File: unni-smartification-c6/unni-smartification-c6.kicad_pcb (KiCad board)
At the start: 4 copper layers, 83.3 x 65 mm, 74 parts, among them J1 USB-C (replacement daughterbo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, J10 Conn_01x06, J2 Li-Ion 1S JST-PH, J3 Conn_01x06, J4 UNNI DC / battery input - AC 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, J5 Conn_01x02, J6 Conn_01x05, Q1 AO3401A, Q10 AO3400A touch emulator, Q2 AO3401A, Q3 AO3400A, Q4 AO3400A, SW1 RESET, SW2 BOOT, U1 MCP73831T-2ACI/OT, U10 ESP32-C6-MINI-1, U2 TPS63031DSK, U3 TPS613222ADBZ (5V), U4 TPD2E009DBZR

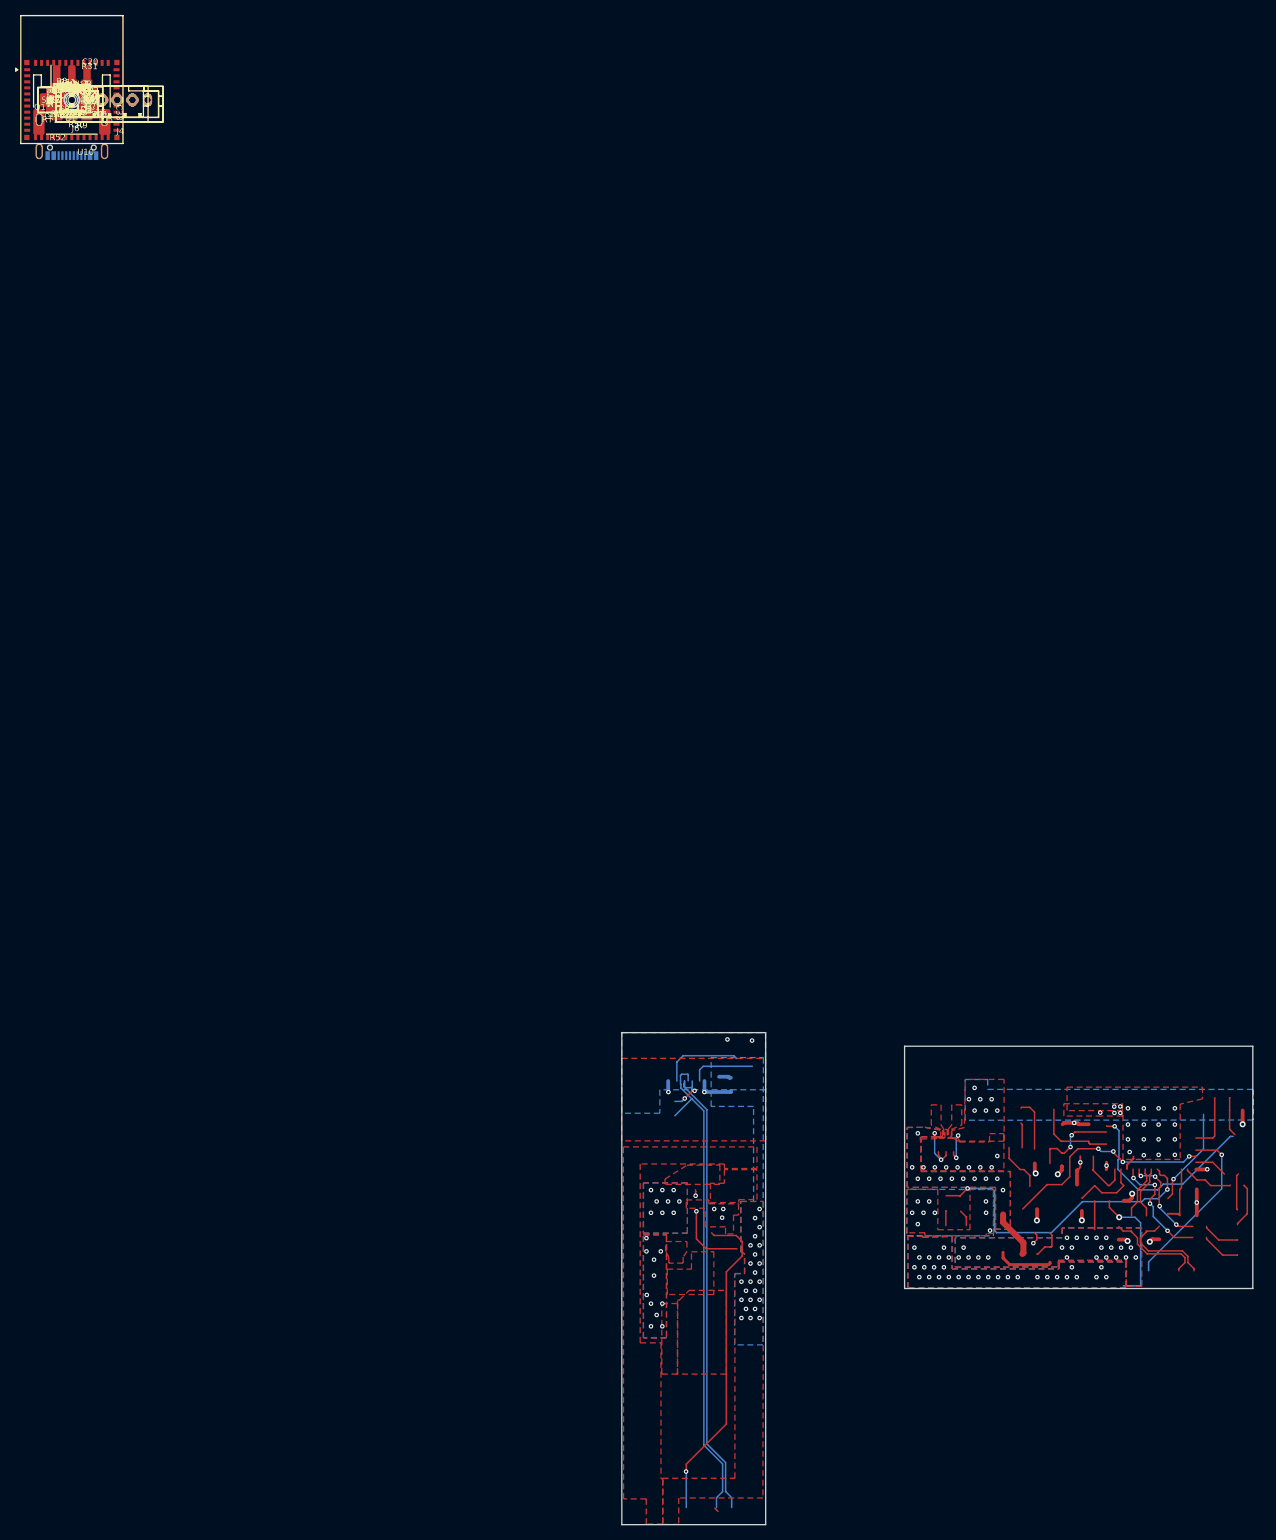
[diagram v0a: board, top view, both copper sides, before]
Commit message: beautify silkscreen on pcbs
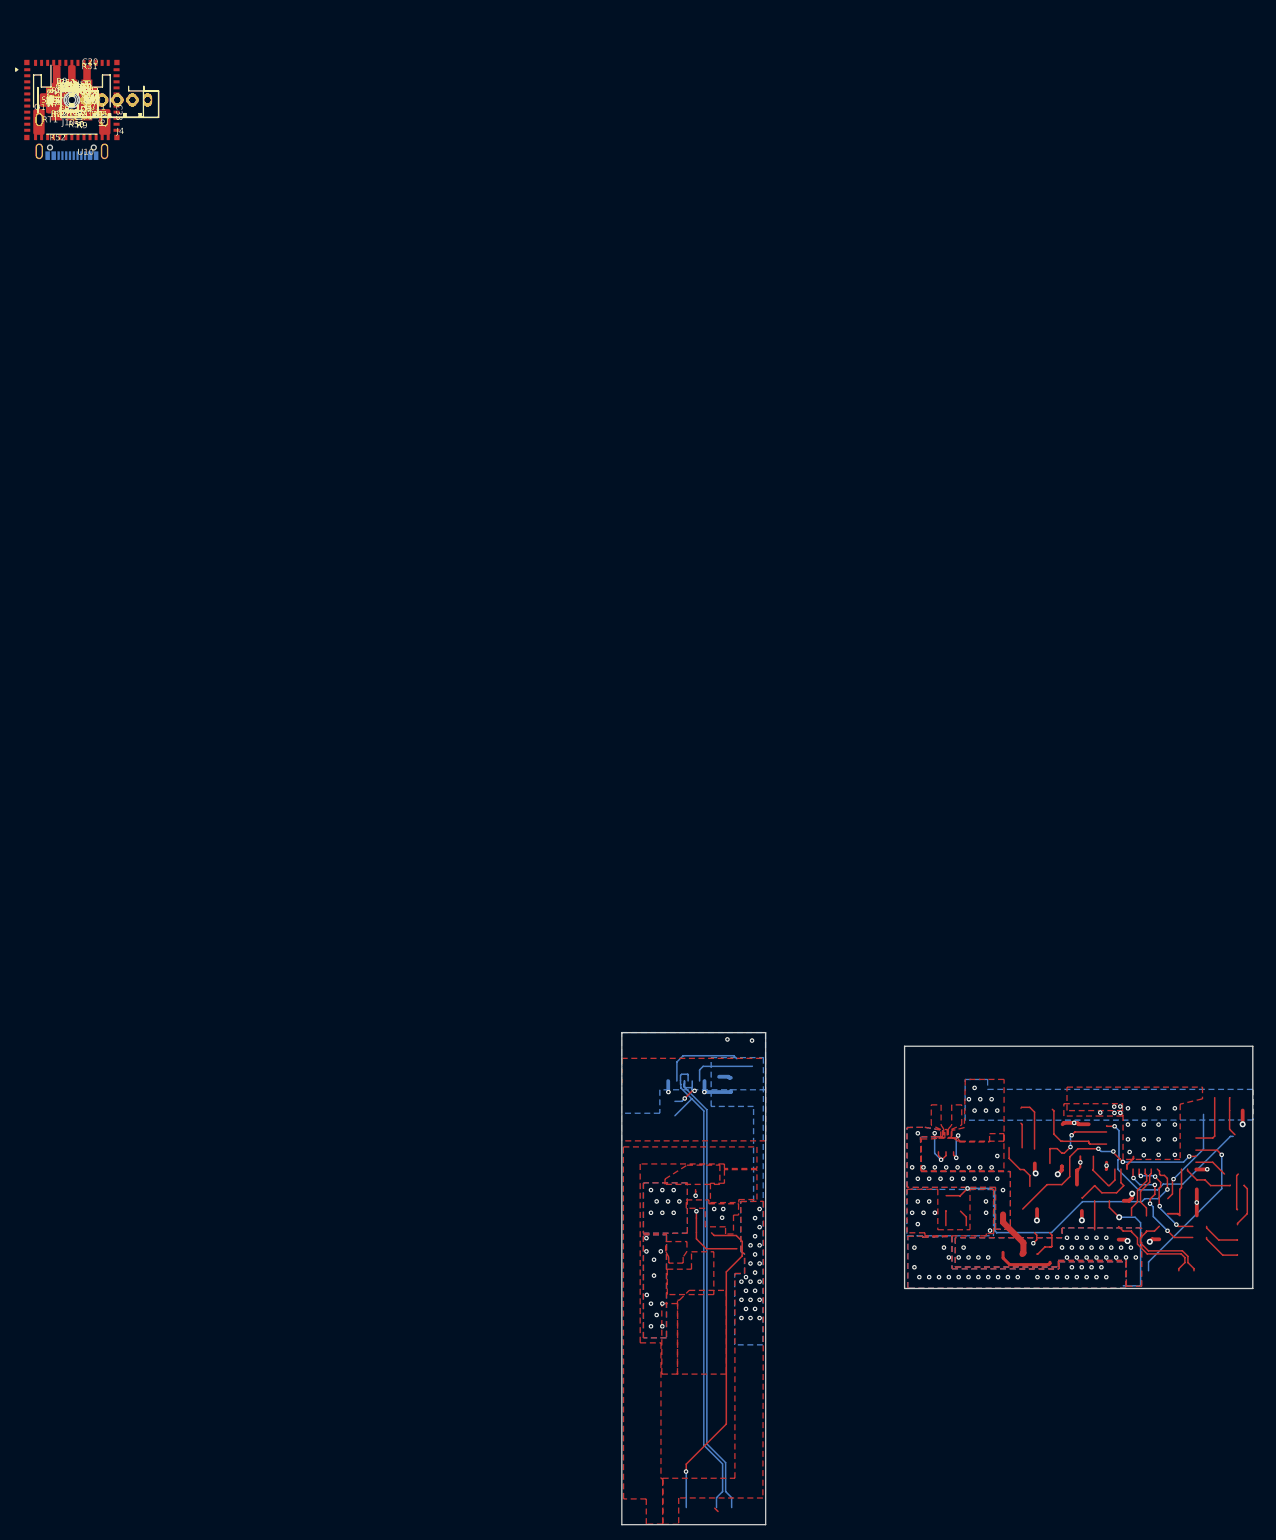
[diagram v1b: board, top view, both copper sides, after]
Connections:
- C13 pad 1: USB_RAW_P -> GND
- J1 pad A6: USB_RAW_P -> GND
- J1 pad B6: USB_RAW_P -> GND
- J10 pad 1: USB_RAW_P -> GND
- J3 pad 1: USB_RAW_P -> GND
- Q1 pad 1: Net-(Q1-G) -> SYS
- R23 pad 2: USB_RAW_P -> GND
- R5 pad 2: Net-(Q1-G) -> SYS
- R6 pad 2: Net-(Q1-G) -> SYS
- U4 pad 1: USB_RAW_P -> GND
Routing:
- net USB_RAW_P: track 78.7 -> 0.00 mm, vias 2 -> 0
- net GND: track 30.4 -> 109.1 mm, vias 63 -> 65
- net Net-(Q1-G): track 4.37 -> 0.00 mm
- net SYS: track 12.4 -> 16.8 mm
- net VBUS: vias 47 -> 52
- net +BATT: vias 31 -> 28

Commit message: silkscreen beautification
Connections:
- C13 pad 1: GND -> USB_RAW_P
- J1 pad A6: GND -> USB_RAW_P
- J1 pad B6: GND -> USB_RAW_P
- J10 pad 1: GND -> USB_RAW_P
- J3 pad 1: GND -> USB_RAW_P
- Q1 pad 1: SYS -> Net-(Q1-G)
- R23 pad 2: GND -> USB_RAW_P
- R5 pad 2: SYS -> Net-(Q1-G)
- R6 pad 2: SYS -> Net-(Q1-G)
- U4 pad 1: GND -> USB_RAW_P
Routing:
- net USB_RAW_P: track 0.00 -> 78.7 mm, vias 0 -> 2
- net GND: track 109.1 -> 30.4 mm, vias 65 -> 63
- net Net-(Q1-G): track 0.00 -> 4.37 mm
- net SYS: track 16.8 -> 12.4 mm
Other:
- board text added: "B-B+"
- board text added: "GND RT RH SDA SCL"
- board text added: "LED TOUCH"

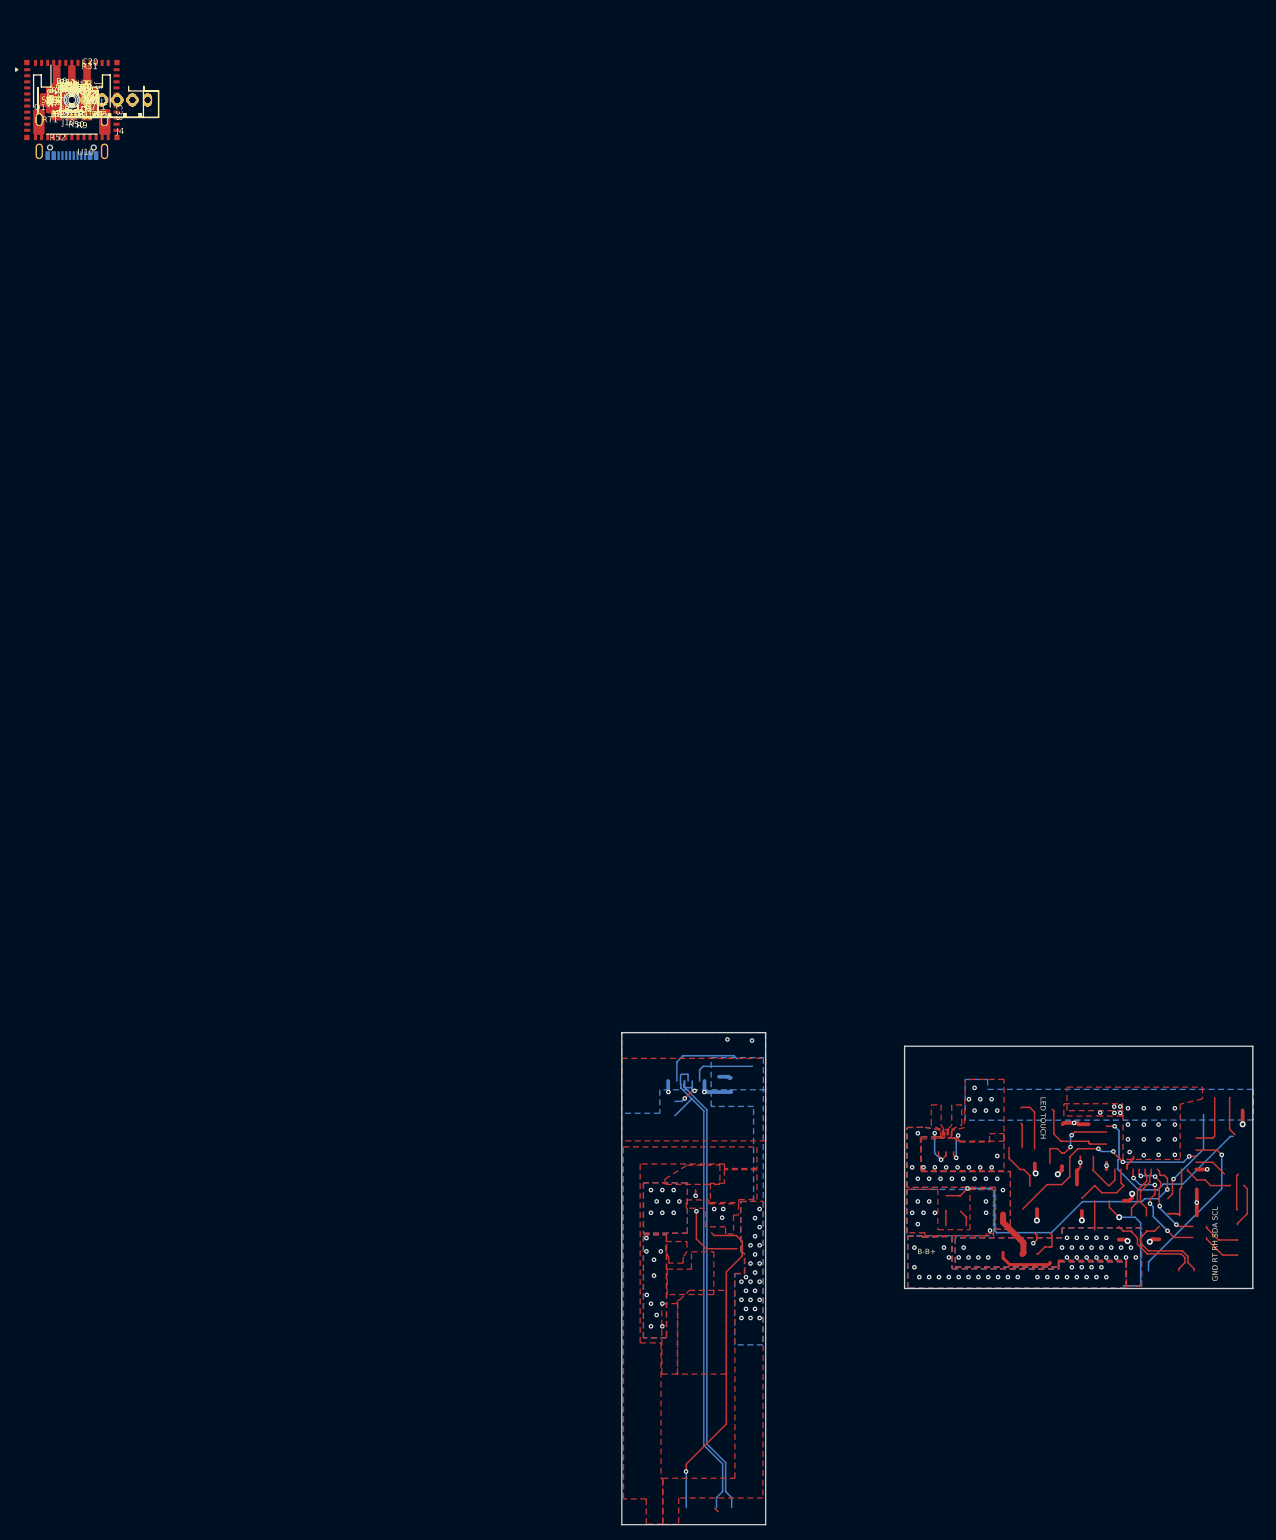
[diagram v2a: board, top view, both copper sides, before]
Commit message: redid some routing, add btn for manual measurements from unni
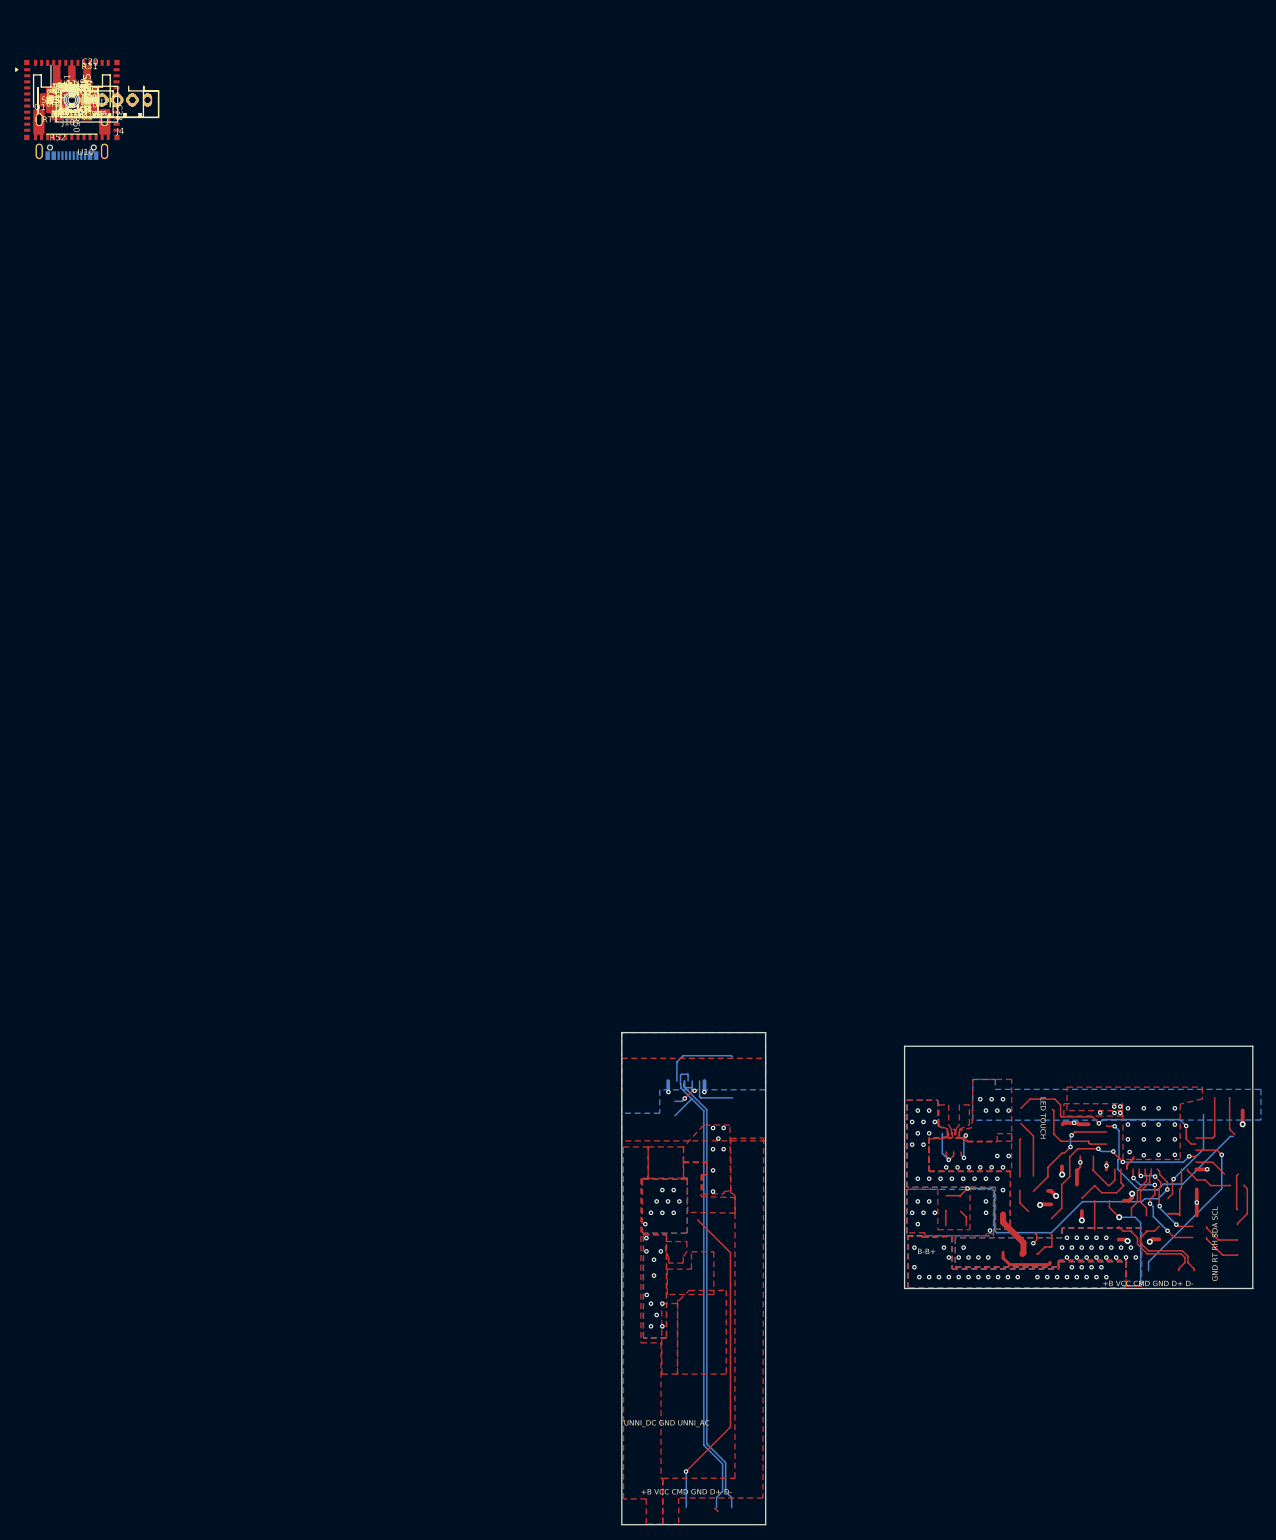
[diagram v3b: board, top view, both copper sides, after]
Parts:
- J5: footprint Connector_JST:JST_PH_B2B-PH-K_1x02_P2.00mm_Vertical -> Connector_JST:JST_PH_B3B-PH-K_1x03_P2.00mm_Vertical
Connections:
- U10 pad 28: unconnected-(U10-IO22-Pad28) -> CONN_BTN
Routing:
- net CONN_BTN: track 0.00 -> 28.3 mm, vias 0 -> 2
- net Net-(Q3-G): track 12.4 -> 0.00 mm, vias 2 -> 0
- net VBUS: track 18.0 -> 14.3 mm, vias 52 -> 28
- net Net-(Q10-D): track 6.56 -> 3.31 mm
- net BACKLIGHT_ADC: track 11.7 -> 14.5 mm
- net Net-(J1-CC2): track 8.64 -> 6.48 mm
- net CONN_TOUCH: track 3.31 -> 5.13 mm
- net GND: track 30.4 -> 28.6 mm, vias 63 -> 65
- net TOUCH_TRIGGER: track 28.8 -> 27.4 mm
- net Net-(J1-CC1): track 11.0 -> 10.3 mm
- net CONN_LED+: track 6.98 -> 7.65 mm
- net SYS: vias 13 -> 19
- net +3V3: vias 15 -> 14
- added copper zone on F.Cu, net Net-(Q3-G)
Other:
- board text added: "+B VCC CMD GND D+ D-"
- board text added: "UNNI_DC GND UNNI_AC"

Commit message: some silkscreen changes
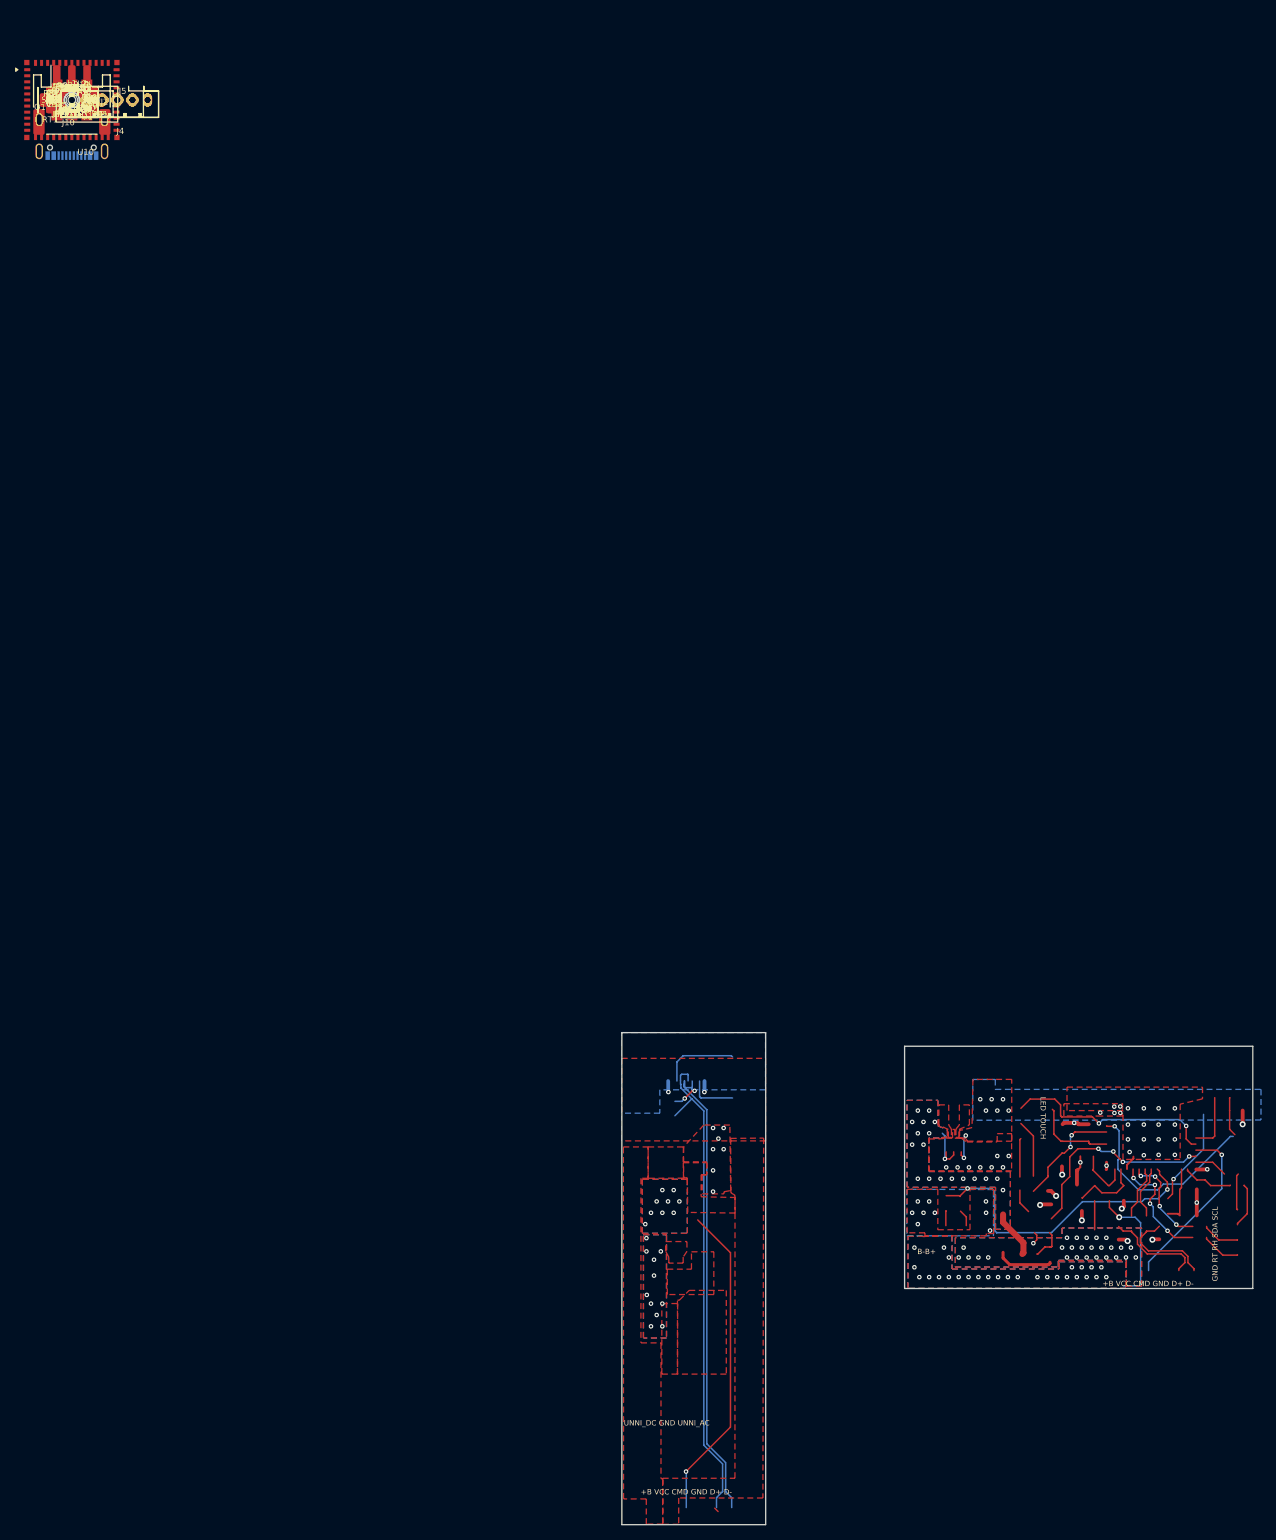
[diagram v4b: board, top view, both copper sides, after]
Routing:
- net GND: track 28.6 -> 27.5 mm
